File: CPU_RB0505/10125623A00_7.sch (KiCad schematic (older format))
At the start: 71 parts, among them IC20 SN74LVC1G07DBVT, IC6 SN74LVC1G07DBVT, J1 ZIF-52610-2290, J17 FH_40BR, J3 , J6 87606-408, J7 26BR-HE10, T1 2N7002, T16 IRLML5103, T2 2N7002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

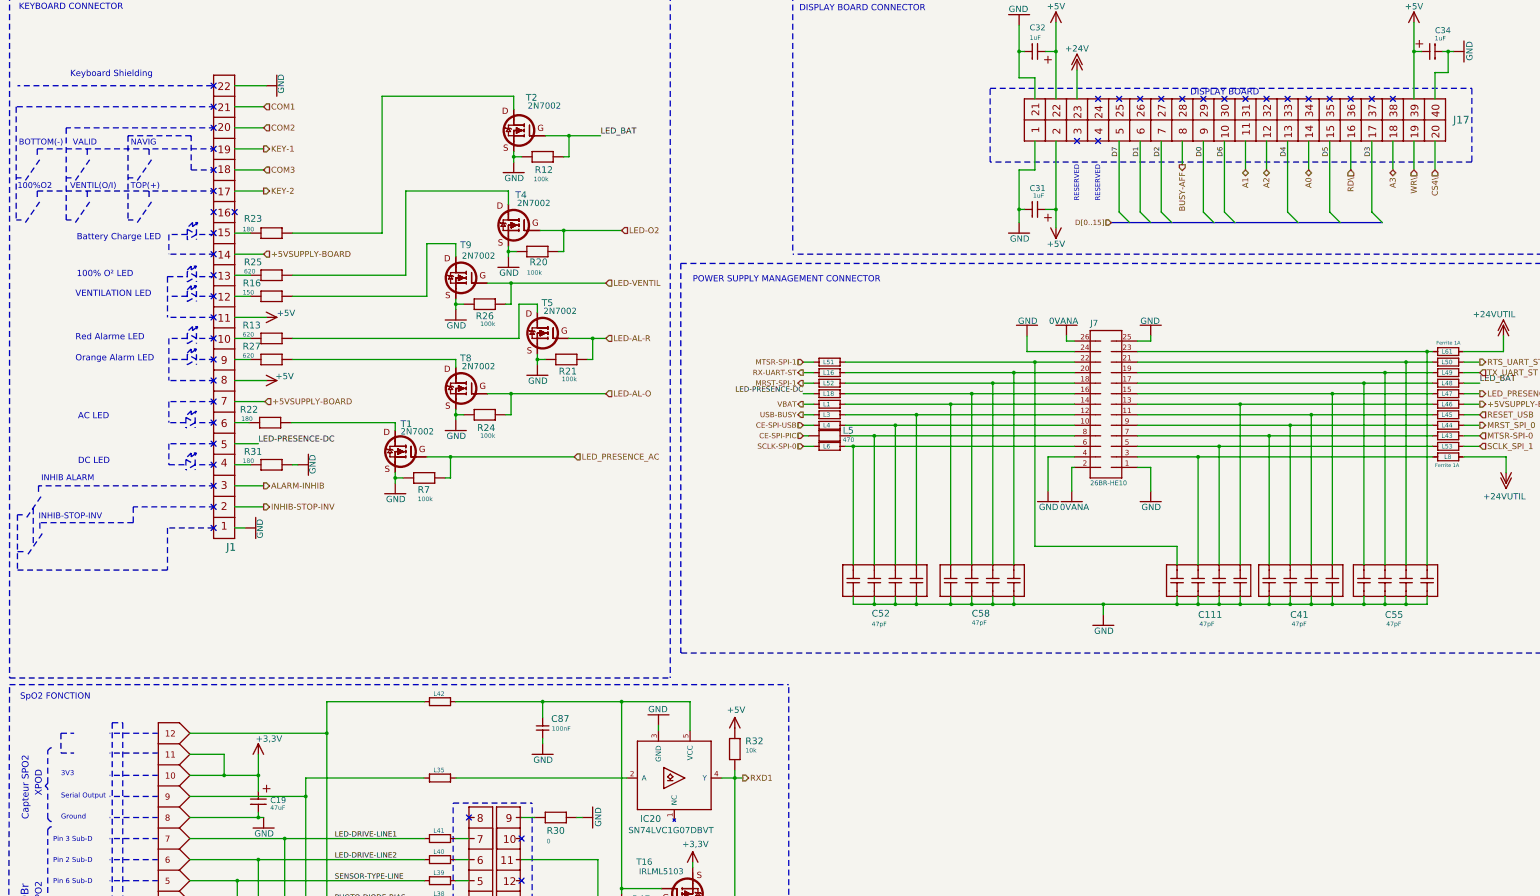
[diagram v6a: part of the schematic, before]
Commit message: Fixed issues in review sheet 7
 (except visual-only changes to symbols that will be replaced later by Kicad symbols)
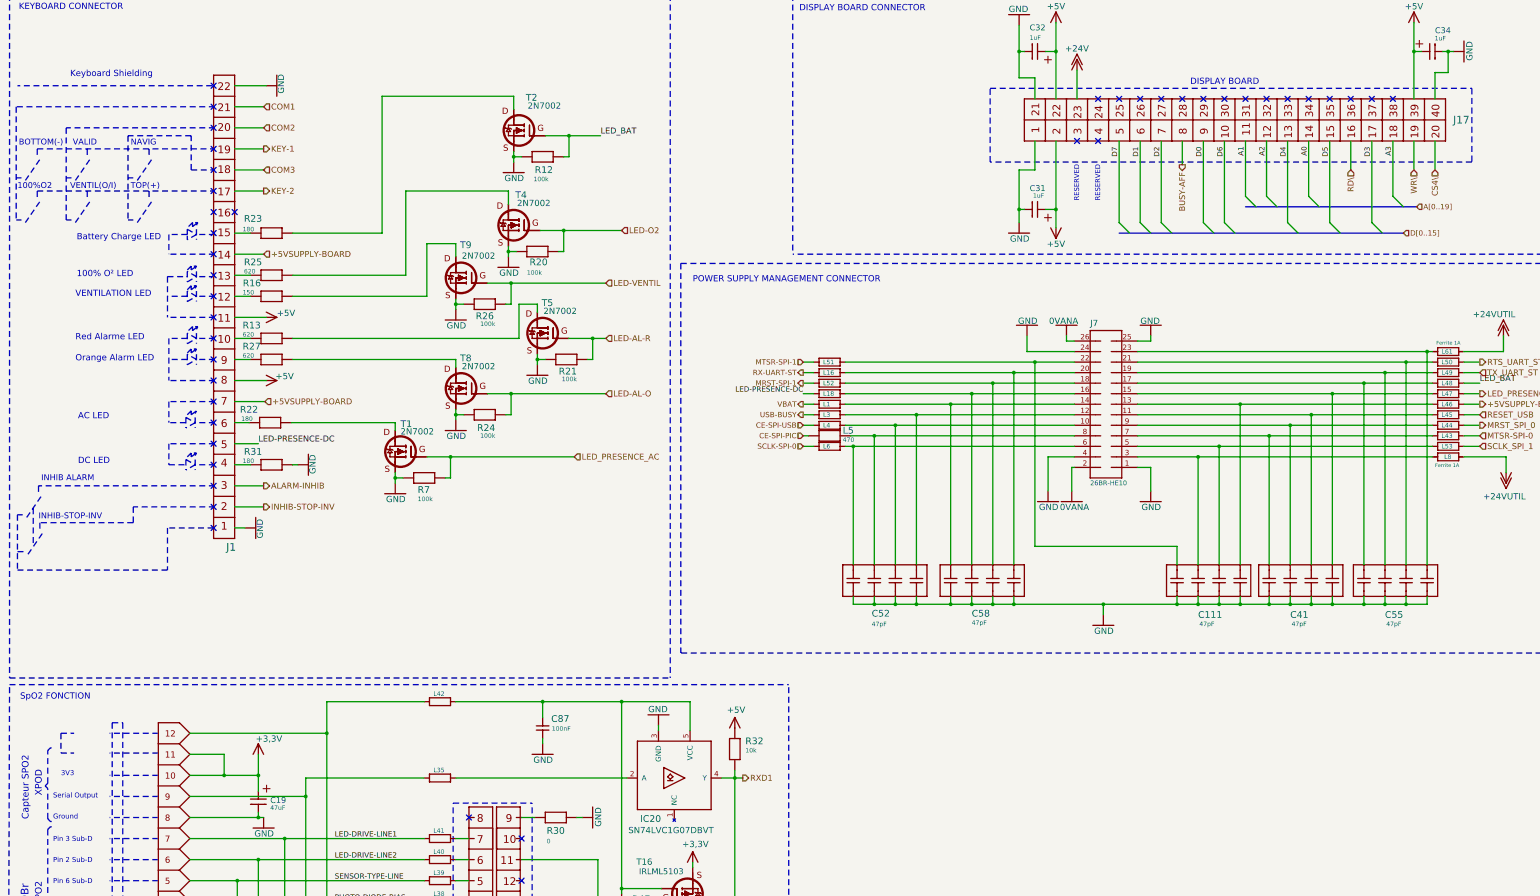
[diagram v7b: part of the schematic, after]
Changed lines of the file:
@@
 $Descr User 17335 11946
 encoding utf-8
-Sheet 8 8
+Sheet 6 8
 Title "RB0505 CPU Board"
 Date ""
@@
 Text HLabel 12000 2375 3    56   Output ~ 0
 BUSY-AFF
-Text HLabel 13200 2425 3    56   BiDi ~ 0
-A0
-Text HLabel 12600 2425 3    56   BiDi ~ 0
-A1
-Text HLabel 12800 2425 3    56   BiDi ~ 0
-A2
-Text HLabel 14000 2425 3    56   BiDi ~ 0
-A3
 Text HLabel 13600 2425 3    56   Input ~ 0
 RD\
@@
 Text Notes 1350 8188 0    47   ~ 0
 3V3
-Text Notes 1350 8400 0    47   ~ 0
+Text Notes 1275 8400 0    47   ~ 0
 Serial Output
-Text Notes 1350 8600 0    47   ~ 0
+Text Notes 1275 8600 0    47   ~ 0
 Ground
 Text Notes 1175 9800 1    64   ~ 0
@@
 Text Notes 5225 10400 0    59   ~ 0
 Carte SPO2
-Text Notes 12075 1725 0    59   ~ 0
+Text Notes 12075 1625 0    59   ~ 0
 DISPLAY BOARD
 Wire Notes Line
@@
 	14200 2150 14200 2425
 Wire Wire Line
-	14000 2150 14000 2425
-Wire Wire Line
-	13800 2150 13800 2825
+	14000 2150 14000 2675
+Wire Wire Line
+	13800 2150 13800 2925
 Wire Wire Line
 	13600 2150 13600 2425
 Wire Wire Line
-	13200 2150 13200 2425
-Wire Wire Line
-	13000 2150 13000 2825
-Wire Wire Line
-	12800 2150 12800 2425
-Wire Wire Line
-	12600 2150 12600 2425
-Wire Wire Line
-	12400 2150 12400 2825
-Wire Wire Line
-	12200 2150 12200 2825
+	13200 2150 13200 2675
+Wire Wire Line
+	13000 2150 13000 2925
+Wire Wire Line
+	12800 2150 12800 2675
+Wire Wire Line
+	12600 2150 12600 2675
+Wire Wire Line
+	12400 2150 12400 2925
+Wire Wire Line
+	12200 2150 12200 2925
 Wire Wire Line
 	12000 2150 12000 2375
 Wire Wire Line
-	11800 2150 11800 2825
-Wire Wire Line
-	11600 2150 11600 2825
-Wire Wire Line
-	11400 2150 11400 2825
+	11800 2150 11800 2925
+Wire Wire Line
+	11600 2150 11600 2925
+Wire Wire Line
+	11400 2150 11400 2925
 Wire Wire Line
 	10800 2150 10800 2800
@@
 D7
 Entry Wire Line
-	11400 2825 11500 2925
+	11400 2925 11500 3025
 Entry Wire Line
-	11600 2825 11700 2925
+	11600 2925 11700 3025
 Entry Wire Line
-	11800 2825 11900 2925
+	11800 2925 11900 3025
 Entry Wire Line
-	12200 2825 12300 2925
+	12200 2925 12300 3025
 Entry Wire Line
-	12400 2825 12500 2925
+	12400 2925 12500 3025
 Entry Wire Line
-	13000 2825 13100 2925
+	13000 2925 13100 3025
 Entry Wire Line
-	13400 2825 13500 2925
+	13400 2925 13500 3025
 Entry Wire Line
-	13800 2825 13900 2925
-Text HLabel 11325 2925 0    50   Input ~ 0
+	13800 2925 13900 3025
+Text HLabel 14100 3025 2    50   Input ~ 0
 D[0..15]
 Wire Wire Line
-	13400 2150 13400 2825
+	13400 2150 13400 2925
 NoConn ~ 2800 5425
 NoConn ~ 2800 5625
 NoConn ~ 2800 5825
+Entry Wire Line
+	12600 2675 12700 2775
+Entry Wire Line
+	12800 2675 12900 2775
+Entry Wire Line
+	13200 2675 13300 2775
+Entry Wire Line
+	14000 2675 14100 2775
+Text Label 12600 2200 3    50   ~ 0
+A1
+Text Label 12800 2200 3    50   ~ 0
+A2
+Text Label 13200 2200 3    50   ~ 0
+A0
+Text Label 14000 2200 3    50   ~ 0
+A3
+Text HLabel 14225 2775 2    50   Input ~ 0
+A[0..19]
 Wire Bus Line
-	11325 2925 13900 2925
+	12600 2775 14225 2775
+Wire Bus Line
+	11400 3025 14100 3025
 $EndSCHEMATC
